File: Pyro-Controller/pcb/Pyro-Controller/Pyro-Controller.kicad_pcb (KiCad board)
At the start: 2 copper layers, 26.9 x 26.9 mm, 13 parts, among them J1 Screw_Terminal_01x02, J2 Conn_01x03_Socket, Q1 SiS454DN

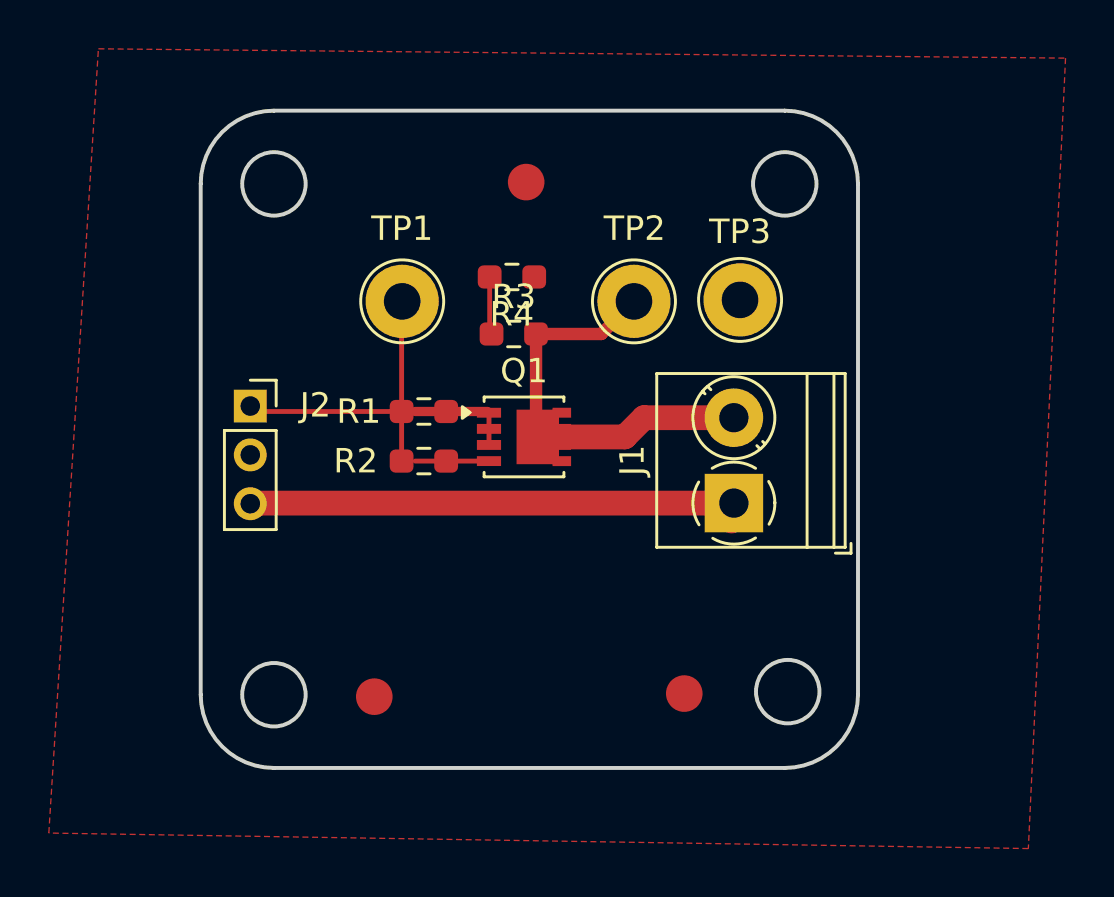
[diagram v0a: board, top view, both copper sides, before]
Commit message: Added fiducials and repositioned the reference designators.
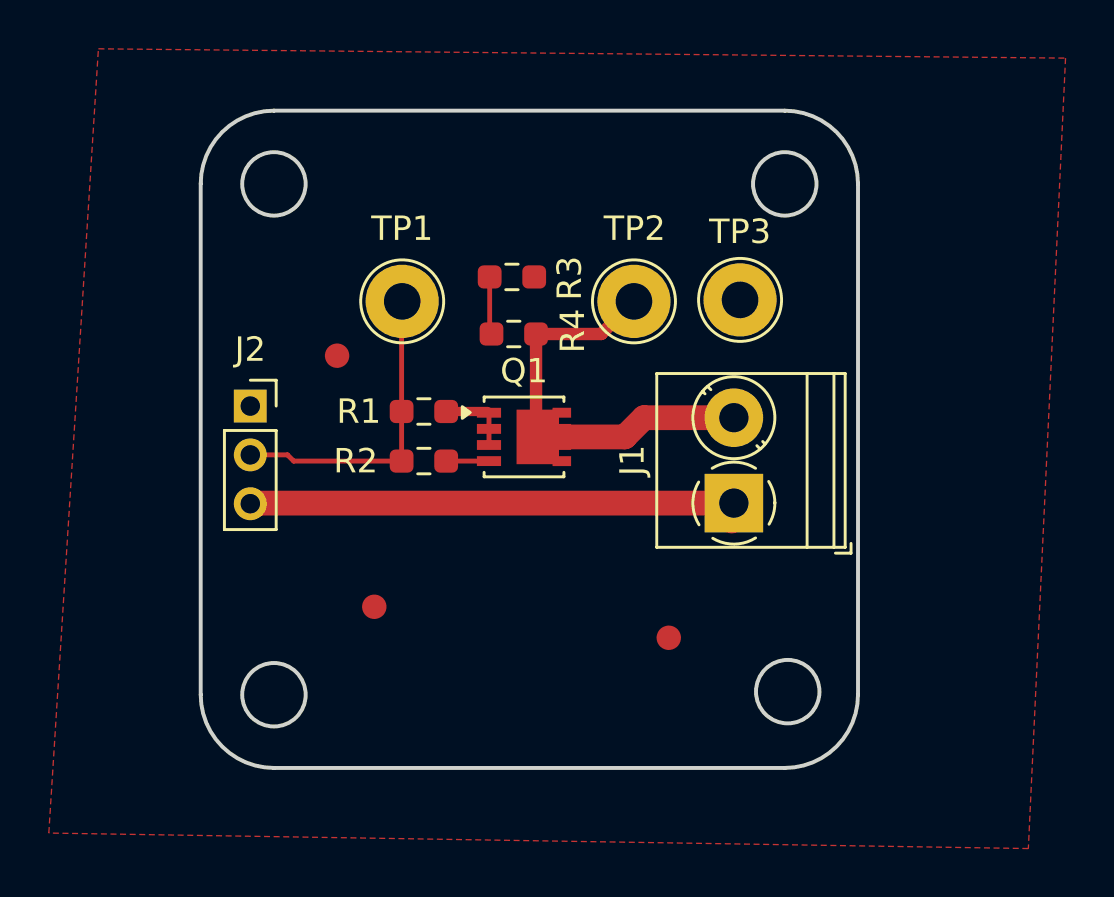
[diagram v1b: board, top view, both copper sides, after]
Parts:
- removed the REF** at (30.7, 41.5)
- removed the REF** at (43.4, 41.4)
- removed the REF** at (37.0, 20.4)
- added REF**: Fiducial_1mm_Mask2mm, Fiducial:Fiducial_1mm_Mask2mm, F.Cu at (42.8, 39.1)
- added REF**: Fiducial_1mm_Mask2mm, Fiducial:Fiducial_1mm_Mask2mm, F.Cu at (29.2, 27.6)
- added REF**: Fiducial_1mm_Mask2mm, Fiducial:Fiducial_1mm_Mask2mm, F.Cu at (30.7, 37.8)
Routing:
- net Net-(Q1-G): track 3.02 -> 1.75 mm
- net GNDD: track 4.37 -> 3.11 mm
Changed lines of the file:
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@@
 	(net 5 "/PyroController/Input")
 	(net 6 "Net-(R3-Pad2)")
+	(footprint "Fiducial:Fiducial_1mm_Mask2mm"
+		(layer "F.Cu")
+		(at 42.799 39.116)
+		(descr "Circular Fiducial, 1mm bare copper, 2mm soldermask opening (Level A)")
+		(tags "fiducial")
+		(property "Reference" "REF**"
+			(at 0 -2 0)
+			(layer "F.SilkS")
+			(hide yes)
+			(effects
+				(font
+					(size 1 1)
+					(thickness 0.15)
+				)
+			)
+		)
+		(property "Value" "Fiducial_1mm_Mask2mm"
+			(at 0 2 0)
+			(layer "F.Fab")
+			(effects
+				(font
+					(size 1 1)
+					(thickness 0.15)
+				)
+			)
+		)
+		(property "Footprint" "Fiducial:Fiducial_1mm_Mask2mm"
+			(at 0 0 0)
+			(unlocked yes)
+			(layer "F.Fab")
+			(hide yes)
+			(effects
+				(font
+					(size 1.27 1.27)
+					(thickness 0.15)
+				)
+			)
+		)
+		(property "Datasheet" ""
+			(at 0 0 0)
+			(unlocked yes)
+			(layer "F.Fab")
+			(hide yes)
+			(effects
+				(font
+					(size 1.27 1.27)
+					(thickness 0.15)
+				)
+			)
+		)
+		(property "Description" ""
+			(at 0 0 0)
+			(unlocked yes)
+			(layer "F.Fab")
+			(hide yes)
+			(effects
+				(font
+					(size 1.27 1.27)
+					(thickness 0.15)
+				)
+			)
+		)
+		(attr smd)
+		(fp_circle
+			(center 0 0)
+			(end 1.25 0)
+			(stroke
+				(width 0.05)
+				(type solid)
+			)
+			(fill none)
+			(layer "F.CrtYd")
+		)
+		(fp_circle
+			(center 0 0)
+			(end 1 0)
+			(stroke
+				(width 0.1)
+				(type solid)
+			)
+			(fill none)
+			(layer "F.Fab")
+		)
+		(fp_text user "${REFERENCE}"
+			(at 0 0 0)
+			(layer "F.Fab")
+			(effects
+				(font
+					(size 0.4 0.4)
+					(thickness 0.06)
+				)
+			)
+		)
+		(pad "" smd circle
+			(at 0 0)
+			(size 1 1)
+			(layers "F.Cu" "F.Mask")
+			(solder_mask_margin 0.5)
+			(clearance 0.5)
+		)
+	)
 	(footprint "Resistor_SMD:R_0603_1608Metric_Pad0.98x0.95mm_HandSolder"
 		(layer "F.Cu")
@@
 		(tags "resistor handsolder")
 		(property "Reference" "R3"
-			(at 0 1.524 0)
+			(at -2.286 2.286 -90)
 			(layer "F.SilkS")
 			(effects
@@
 		(tags "Through hole socket strip THT 1x03 2.00mm single row")
 		(property "Reference" "J2"
-			(at 2.667 -0.032 0)
+			(at 0 -2.318 0)
 			(layer "F.SilkS")
 			(effects
@@
 		(tags "resistor handsolder")
 		(property "Reference" "R4"
-			(at 0 -1.524 0)
+			(at -2.489 -2.21 90)
 			(layer "F.SilkS")
 			(effects
@@
 				(xyz 0 0 0)
 			)
-		)
-	)
-	(footprint "Fiducial:Fiducial_1.5mm_Mask3mm"
-		(layer "F.Cu")
-		(at 30.734 41.529)
-		(descr "Circular Fiducial, 1.5mm bare copper, 3mm soldermask opening")
-		(tags "fiducial")
-		(property "Reference" "REF**"
-			(at 0 -2.4765 0)
-			(layer "F.SilkS")
-			(hide yes)
-			(effects
-				(font
-					(size 1 1)
-					(thickness 0.15)
-				)
-			)
-		)
-		(property "Value" "Fiducial_1.5mm_Mask3mm"
-			(at 0 2.6035 0)
-			(layer "F.Fab")
-			(hide yes)
-			(effects
-				(font
-					(size 1 1)
-					(thickness 0.15)
-				)
-			)
-		)
-		(property "Footprint" "Fiducial:Fiducial_1.5mm_Mask3mm"
-			(at 0 0 0)
-			(unlocked yes)
-			(layer "F.Fab")
-			(hide yes)
-			(effects
-				(font
-					(size 1.27 1.27)
-					(thickness 0.15)
-				)
-			)
-		)
-		(property "Datasheet" ""
-			(at 0 0 0)
-			(unlocked yes)
-			(layer "F.Fab")
-			(hide yes)
-			(effects
-				(font
-					(size 1.27 1.27)
-					(thickness 0.15)
-				)
-			)
-		)
-		(property "Description" ""
-			(at 0 0 0)
-			(unlocked yes)
-			(layer "F.Fab")
-			(hide yes)
-			(effects
-				(font
-					(size 1.27 1.27)
-					(thickness 0.15)
-				)
-			)
-		)
-		(attr smd)
-		(fp_circle
-			(center 0 0)
-			(end 1.75 0)
-			(stroke
-				(width 0.05)
-				(type solid)
-			)
-			(fill none)
-			(layer "F.CrtYd")
-		)
-		(fp_circle
-			(center 0 0)
-			(end 1.5 0)
-			(stroke
-				(width 0.1)
-				(type solid)
-			)
-			(fill none)
-			(layer "F.Fab")
-		)
-		(fp_text user "${REFERENCE}"
-			(at 0 0 0)
-			(layer "F.Fab")
-			(effects
-				(font
-					(size 0.4 0.4)
-					(thickness 0.06)
-				)
-			)
-		)
-		(pad "" smd circle
-			(at 0 0)
-			(size 1.5 1.5)
-			(layers "F.Cu" "F.Mask")
-			(solder_mask_margin 0.75)
-			(clearance 0.75)
 		)
 	)
@@
 		)
 	)
-	(footprint "Fiducial:Fiducial_1.5mm_Mask3mm"
-		(layer "F.Cu")
-		(at 43.434 41.402)
-		(descr "Circular Fiducial, 1.5mm bare copper, 3mm soldermask opening")
+	(footprint "Fiducial:Fiducial_1mm_Mask2mm"
+		(layer "F.Cu")
+		(at 29.21 27.559)
+		(descr "Circular Fiducial, 1mm bare copper, 2mm soldermask opening (Level A)")
 		(tags "fiducial")
 		(property "Reference" "REF**"
-			(at 0 -2.4765 0)
-			(layer "F.SilkS")
-			(hide yes)
-			(effects
-				(font
-					(size 1 1)
-					(thickness 0.15)
-				)
-			)
-		)
-		(property "Value" "Fiducial_1.5mm_Mask3mm"
-			(at 0 2.6035 0)
-			(layer "F.Fab")
-			(hide yes)
-			(effects
-				(font
-					(size 1 1)
-					(thickness 0.15)
-				)
-			)
-		)
-		(property "Footprint" "Fiducial:Fiducial_1.5mm_Mask3mm"
+			(at 0 -2 0)
+			(layer "F.SilkS")
+			(hide yes)
+			(effects
+				(font
+					(size 1 1)
+					(thickness 0.15)
+				)
+			)
+		)
+		(property "Value" "Fiducial_1mm_Mask2mm"
+			(at 0 2 0)
+			(layer "F.Fab")
+			(effects
+				(font
+					(size 1 1)
+					(thickness 0.15)
+				)
+			)
+		)
+		(property "Footprint" "Fiducial:Fiducial_1mm_Mask2mm"
 			(at 0 0 0)
 			(unlocked yes)
@@
 		(fp_circle
 			(center 0 0)
-			(end 1.75 0)
+			(end 1.25 0)
 			(stroke
 				(width 0.05)
@@
 		(fp_circle
 			(center 0 0)
-			(end 1.5 0)
+			(end 1 0)
 			(stroke
 				(width 0.1)
@@
 		(pad "" smd circle
 			(at 0 0)
-			(size 1.5 1.5)
+			(size 1 1)
 			(layers "F.Cu" "F.Mask")
-			(solder_mask_margin 0.75)
-			(clearance 0.75)
+			(solder_mask_margin 0.5)
+			(clearance 0.5)
 		)
 	)
@@
 		)
 	)
-	(footprint "Fiducial:Fiducial_1.5mm_Mask3mm"
-		(layer "F.Cu")
-		(at 36.957 20.447)
-		(descr "Circular Fiducial, 1.5mm bare copper, 3mm soldermask opening")
+	(footprint "Fiducial:Fiducial_1mm_Mask2mm"
+		(layer "F.Cu")
+		(at 30.734 37.846)
+		(descr "Circular Fiducial, 1mm bare copper, 2mm soldermask opening (Level A)")
 		(tags "fiducial")
 		(property "Reference" "REF**"
-			(at 0 -2.4765 0)
-			(layer "F.SilkS")
-			(hide yes)
-			(effects
-				(font
-					(size 1 1)
-					(thickness 0.15)
-				)
-			)
-		)
-		(property "Value" "Fiducial_1.5mm_Mask3mm"
-			(at 0 2.6035 0)
-			(layer "F.Fab")
-			(hide yes)
-			(effects
-				(font
-					(size 1 1)
-					(thickness 0.15)
-				)
-			)
-		)
-		(property "Footprint" "Fiducial:Fiducial_1.5mm_Mask3mm"
+			(at 0 -2 0)
+			(layer "F.SilkS")
+			(hide yes)
+			(effects
+				(font
+					(size 1 1)
+					(thickness 0.15)
+				)
+			)
+		)
+		(property "Value" "Fiducial_1mm_Mask2mm"
+			(at 0 2 0)
+			(layer "F.Fab")
+			(effects
+				(font
+					(size 1 1)
+					(thickness 0.15)
+				)
+			)
+		)
+		(property "Footprint" "Fiducial:Fiducial_1mm_Mask2mm"
 			(at 0 0 0)
 			(unlocked yes)
@@
 		(fp_circle
 			(center 0 0)
-			(end 1.75 0)
+			(end 1.25 0)
 			(stroke
 				(width 0.05)
@@
 		(fp_circle
 			(center 0 0)
-			(end 1.5 0)
+			(end 1 0)
 			(stroke
 				(width 0.1)
@@
 		(pad "" smd circle
 			(at 0 0)
-			(size 1.5 1.5)
+			(size 1 1)
 			(layers "F.Cu" "F.Mask")
-			(solder_mask_margin 0.75)
-			(clearance 0.75)
+			(solder_mask_margin 0.5)
+			(clearance 0.5)
 		)
 	)
@@
 	)
 	(segment
-		(start 32.4085 31.877)
+		(start 33.6785 31.877)
 		(end 35.433 31.877)
 		(width 0.2)
 		(layer "F.Cu")
 		(net 2)
+	)
+	(segment
+		(start 33.6785 29.845)
+		(end 35.381 29.845)
+		(width 0.381)
+		(layer "F.Cu")
+		(net 3)
 	)
 	(segment
@@
 	)
 	(segment
-		(start 32.4085 29.845)
-		(end 35.381 29.845)
-		(width 0.381)
+		(start 25.642 29.833)
+		(end 25.654 29.845)
+		(width 0.2)
 		(layer "F.Cu")
 		(net 3)
@@
 	)
 	(segment
-		(start 25.642 29.833)
-		(end 25.654 29.845)
+		(start 27.178 31.623)
+		(end 25.654 31.623)
 		(width 0.2)
 		(layer "F.Cu")
@@
 	)
 	(segment
-		(start 31.8535 29.845)
-		(end 30.5835 29.845)
+		(start 31.8535 31.877)
+		(end 27.432 31.877)
+		(width 0.2)
+		(layer "F.Cu")
+		(net 5)
+	)
+	(segment
+		(start 27.432 31.877)
+		(end 27.178 31.623)
 		(width 0.2)
 		(layer "F.Cu")
@@
 		(width 0.2)
 		(layer "F.Cu")
-		(net 5)
-	)
-	(segment
-		(start 25.654 29.845)
-		(end 30.5835 29.845)
-		(width 0.2)
-		(layer "F.Cu")

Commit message: Finished fiducials, added title and revision
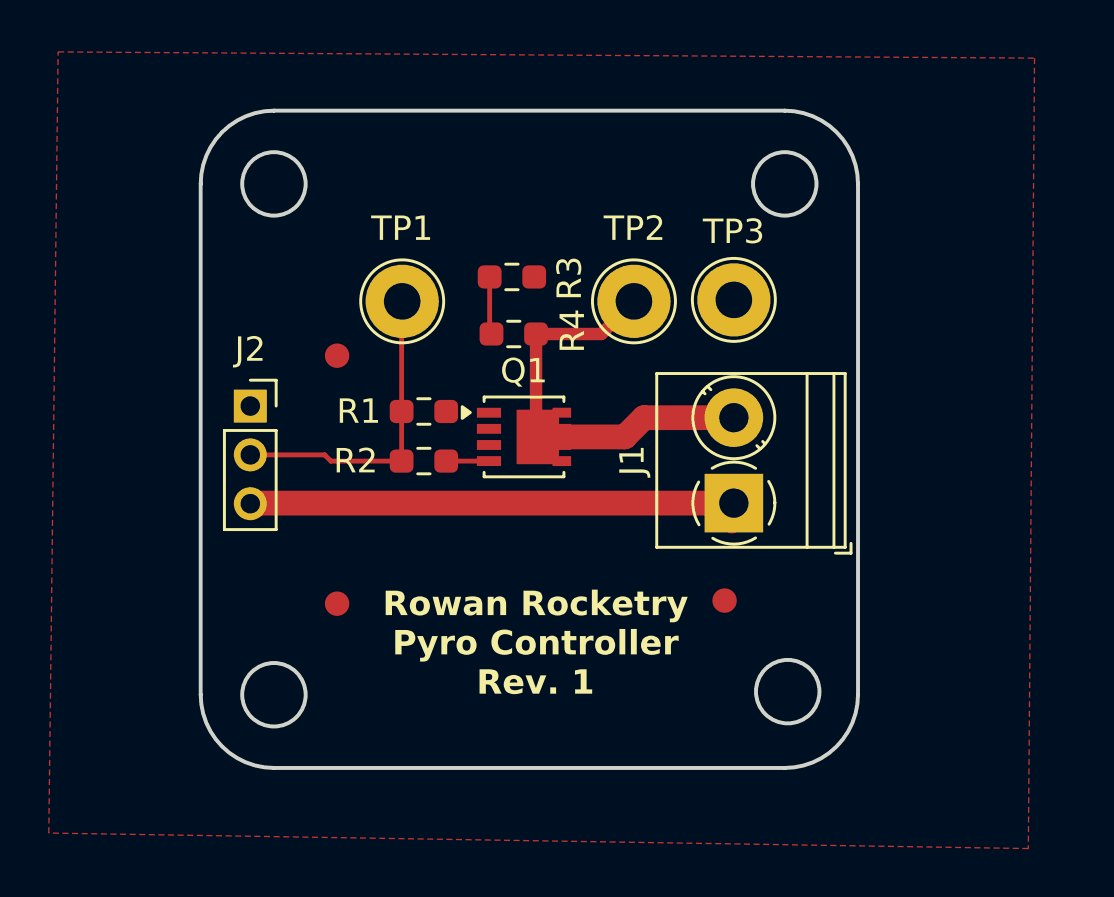
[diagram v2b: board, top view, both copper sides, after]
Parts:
- moved REF** 2.75 mm to (45.1, 37.6)
- moved REF** 1.53 mm to (29.2, 37.7)
- moved TP3 0.25 mm to (45.5, 25.3)
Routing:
- net GNDD: track 3.11 -> 0.09 mm
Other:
- board text added: "Rowan Rocketry Pyro Controller Rev. 1"
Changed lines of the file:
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@@
 	(footprint "Fiducial:Fiducial_1mm_Mask2mm"
 		(layer "F.Cu")
-		(at 42.799 39.116)
+		(at 45.085 37.592)
 		(descr "Circular Fiducial, 1mm bare copper, 2mm soldermask opening (Level A)")
 		(tags "fiducial")
@@
 		(sheetname "PyroController")
 		(sheetfile "PyroController.kicad_sch")
+		(zone_connect 2)
 		(attr smd)
 		(fp_line
@@
 	(footprint "TestPoint:TestPoint_Loop_D2.54mm_Drill1.5mm_Beaded"
 		(layer "F.Cu")
-		(at 45.72 25.273)
+		(at 45.466 25.273)
 		(descr "wire loop with bead as test point, loop diameter2.548mm, hole diameter 1.5mm")
 		(tags "test point wire loop bead")
@@
 	(footprint "Fiducial:Fiducial_1mm_Mask2mm"
 		(layer "F.Cu")
-		(at 30.734 37.846)
+		(at 29.21 37.719)
 		(descr "Circular Fiducial, 1mm bare copper, 2mm soldermask opening (Level A)")
 		(tags "fiducial")
@@
 		(layer "Edge.Cuts")
 	)
+	(gr_text "Rowan Rocketry\nPyro Controller\nRev. 1"
+		(at 37.338 41.529 0)
+		(layer "F.SilkS")
+		(effects
+			(font
+				(size 1 1)
+				(thickness 0.2)
+				(bold yes)
+			)
+			(justify bottom)
+		)
+	)
+	(dimension
+		(type aligned)
+		(layer "F.SilkS")
+		(pts
+			(xy 23.622 20.519742) (xy 50.552258 20.519742)
+		)
+		(height -5.914742)
+		(gr_text "1.0602 in"
+			(at 37.087129 13.505 0)
+			(layer "F.SilkS")
+			(effects
+				(font
+					(size 1 1)
+					(thickness 0.1)
+				)
+			)
+		)
+		(format
+			(prefix "")
+			(suffix "")
+			(units 3)
+			(units_format 1)
+			(precision 4)
+		)
+		(style
+			(thickness 0.1)
+			(arrow_length 1.27)
+			(text_position_mode 0)
+			(extension_height 0.58642)
+			(extension_offset 0.5) keep_text_aligned)
+	)
 	(segment
 		(start 45.466 33.599)
@@
 	)
 	(segment
-		(start 33.6785 29.845)
-		(end 35.381 29.845)
-		(width 0.381)
-		(layer "F.Cu")
-		(net 3)
-	)
-	(segment
-		(start 35.433 31.217)
-		(end 35.433 29.897)
-		(width 0.2)
-		(layer "F.Cu")
-		(net 3)
-	)
-	(segment
 		(start 25.642 29.833)
 		(end 25.654 29.845)
@@
 	)
 	(segment
-		(start 35.381 29.845)
-		(end 35.433 29.897)
+		(start 33.7305 29.897)
+		(end 33.6785 29.845)
 		(width 0.2)
 		(layer "F.Cu")
@@
 	)
 	(segment
+		(start 41.373 25.333)
+		(end 40.036 26.67)
+		(width 0.508)
+		(layer "F.Cu")
+		(net 4)
+	)
+	(segment
 		(start 45.466 30.099)
 		(end 45.373 30.192)
@@
 	)
 	(segment
+		(start 41.783 30.099)
+		(end 40.995 30.887)
+		(width 1.016)
+		(layer "F.Cu")
+		(net 4)
+	)
+	(segment
 		(start 40.036 26.67)
 		(end 37.3615 26.67)
 		(width 0.508)
-		(layer "F.Cu")
-		(net 4)
-	)
-	(segment
-		(start 41.783 30.099)
-		(end 40.995 30.887)
-		(width 1.016)
 		(layer "F.Cu")
 		(net 4)
@@
 	)
 	(segment
-		(start 41.373 25.333)
-		(end 40.036 26.67)
-		(width 0.508)
-		(layer "F.Cu")
-		(net 4)
-	)
-	(segment
 		(start 31.8535 26.3135)
 		(end 31.8535 29.845)
@@
 	)
 	(segment
-		(start 27.178 31.623)
-		(end 25.654 31.623)
-		(width 0.2)
-		(layer "F.Cu")
-		(net 5)
-	)
-	(segment
-		(start 31.8535 31.877)
-		(end 27.432 31.877)
-		(width 0.2)
-		(layer "F.Cu")
-		(net 5)
-	)
-	(segment
-		(start 27.432 31.877)
-		(end 27.178 31.623)
+		(start 28.956 31.877)
+		(end 28.702 31.623)
 		(width 0.2)
 		(layer "F.Cu")
@@
 		(start 31.8535 31.877)
 		(end 31.8535 29.845)
+		(width 0.2)
+		(layer "F.Cu")
+		(net 5)
+	)
+	(segment
+		(start 31.8535 31.877)
+		(end 28.956 31.877)
+		(width 0.2)
+		(layer "F.Cu")
+		(net 5)
+	)
+	(segment
+		(start 28.702 31.623)
+		(end 25.654 31.623)
 		(width 0.2)
 		(layer "F.Cu")
@@
 		(polygon
 			(pts
-				(xy 17.399 47.117) (xy 19.431 14.986) (xy 59.055 15.367) (xy 57.531 47.752)
-			)
-		)
+				(xy 17.399 47.117) (xy 17.78 15.113) (xy 57.785 15.367) (xy 57.531 47.752)
+			)
+		)

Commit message: BOM, BOM Template, Rowan Rocketry Logo
- Finished pyro controller BOM
- Created template for BOMs
- Created a footprint for adding the Rowan Rocketry logo to PCBs
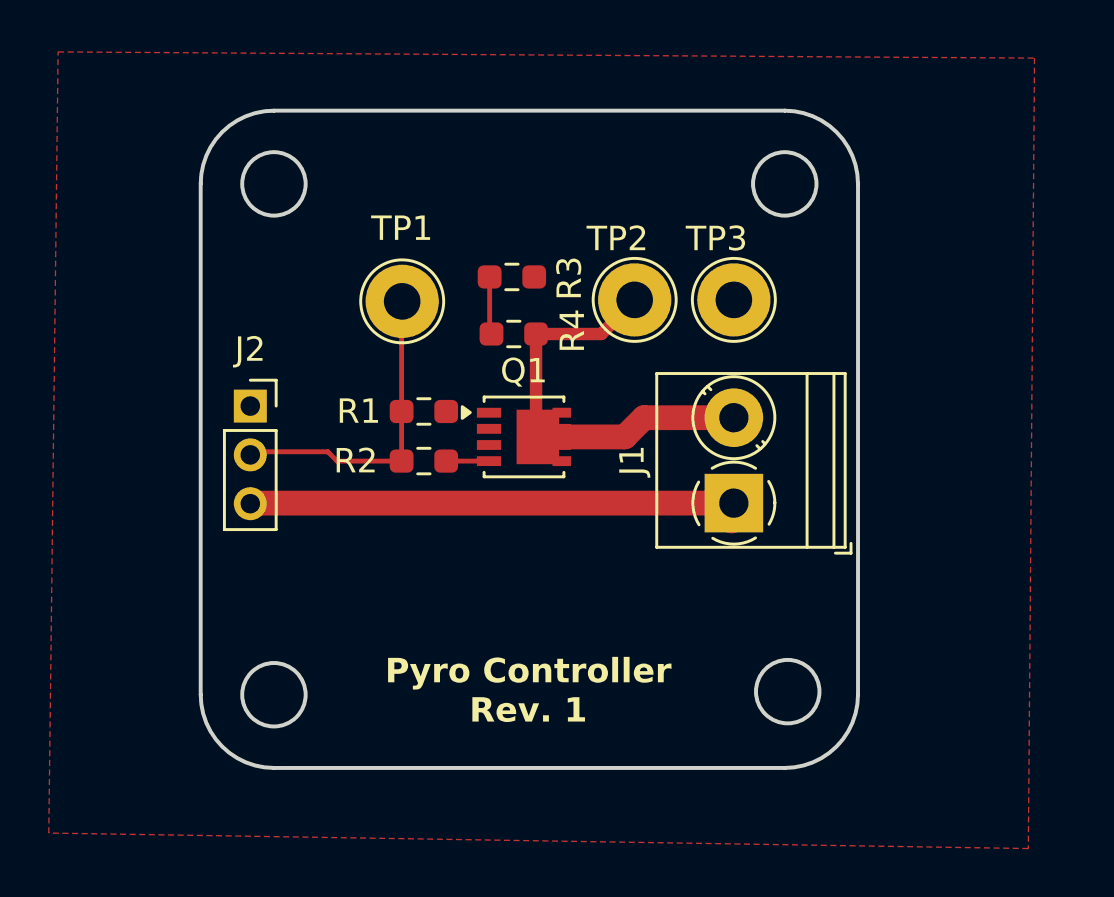
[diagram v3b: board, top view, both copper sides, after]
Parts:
- removed REF** (x3): Fiducial_1mm_Mask2mm, Fiducial:Fiducial_1mm_Mask2mm
- added G***: LOGO, LOGO, B.Cu at (37.5, 34.3)
- moved TP2 0.07 mm to (41.4, 25.3), turned to 180 degrees
- turned TP3 to 180 degrees
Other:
- board text added: "Pyro Controller Rev. 1"
- board text removed: "Rowan Rocketry Pyro Controller Rev. 1"
